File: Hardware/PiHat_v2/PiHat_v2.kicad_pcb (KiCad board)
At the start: 2 copper layers, 64 x 55 mm, 23 parts, among them P1 CONN_02X20, P2 CONN_01X02, P3 CONN_01X08

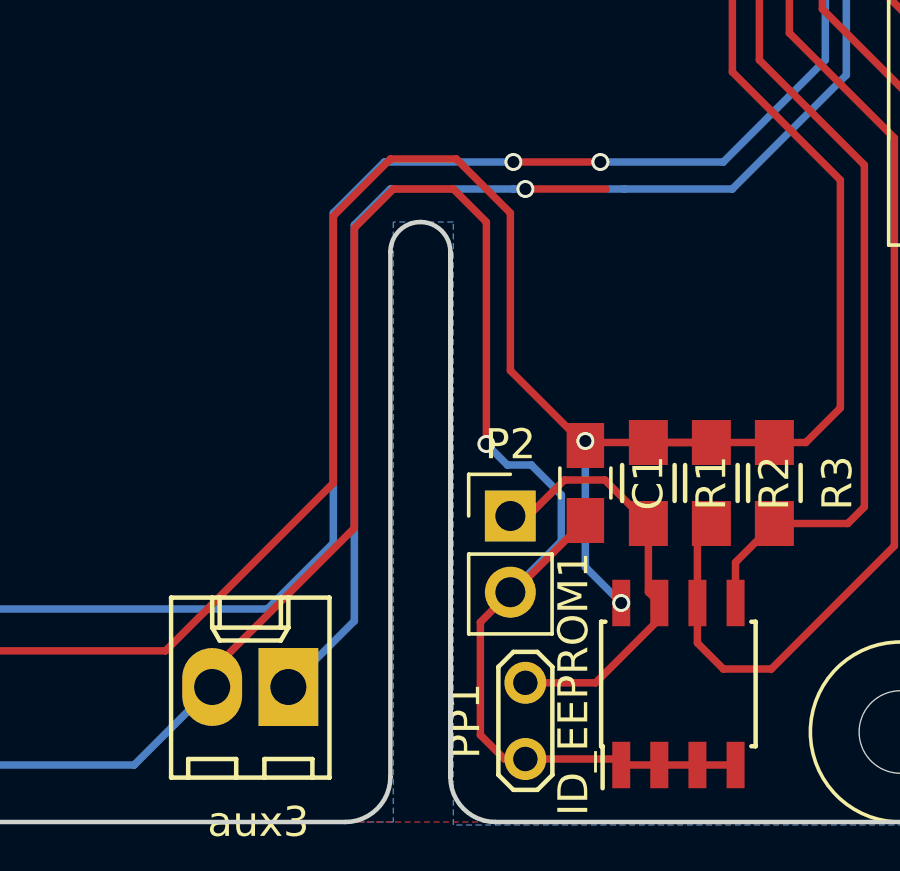
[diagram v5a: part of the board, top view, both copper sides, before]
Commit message: Insert Missing Via
I was missing a via in the lower right of the board - it has now been
re-inserted.
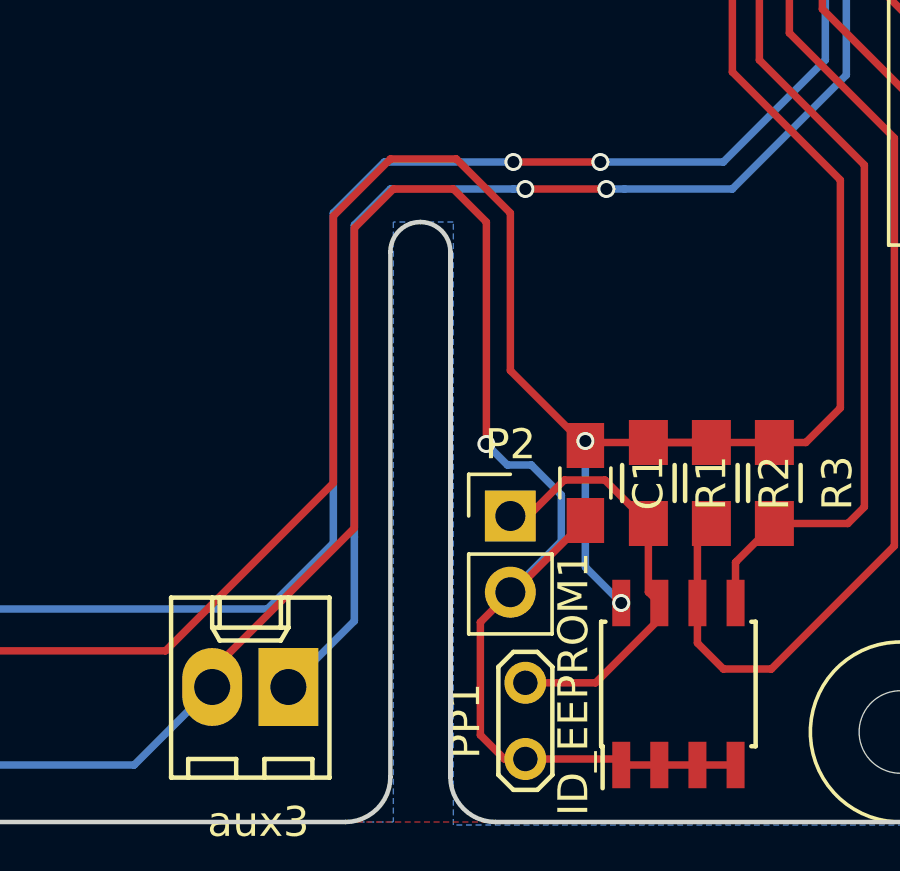
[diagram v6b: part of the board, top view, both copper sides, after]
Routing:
- net /GPIO5: vias 1 -> 2
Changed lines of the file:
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@@
   (general
     (links 56)
-    (no_connects 9)
+    (no_connects 8)
     (area 79.650001 53.1 168.85 129.200001)
     (thickness 1.6)
     (drawings 48)
-    (tracks 245)
+    (tracks 246)
     (zones 0)
     (modules 23)
@@
   (segment (start 96.2 72.2) (end 96.2 72.1) (width 0.25) (layer F.Cu) (net 1))
   (segment (start 96.2 72.1) (end 102 66.3) (width 0.25) (layer F.Cu) (net 1))
+  (segment (start 113.66 72.06) (end 112.16 70.56) (width 0.25) (layer F.Cu) (net 2))
+  (segment (start 112.16 70.56) (end 112.16 66.3) (width 0.25) (layer F.Cu) (net 2))
   (segment (start 118.5 115.1) (end 109.8 115.1) (width 0.25) (layer B.Cu) (net 2))
   (segment (start 109.8 115.1) (end 104.6 109.9) (width 0.25) (layer B.Cu) (net 2))
@@
   (segment (start 141 110.34) (end 142 109.34) (width 0.25) (layer F.Cu) (net 2))
   (segment (start 113.66 72.2) (end 113.66 72.06) (width 0.25) (layer F.Cu) (net 2))
-  (segment (start 113.66 72.06) (end 112.16 70.56) (width 0.25) (layer F.Cu) (net 2))
-  (segment (start 112.16 70.56) (end 112.16 66.3) (width 0.25) (layer F.Cu) (net 2))
   (segment (start 113.66 72.2) (end 113.5 72.2) (width 0.25) (layer B.Cu) (net 2))
   (segment (start 118.5 111.295) (end 114.495 111.295) (width 0.25) (layer F.Cu) (net 4))
@@
   (segment (start 149.1 111.9) (end 148.235 111.035) (width 0.25) (layer F.Cu) (net 22))
   (segment (start 148.235 111.035) (end 148.235 109.7) (width 0.25) (layer F.Cu) (net 22))
+  (via (at 145.2 95.9) (size 0.6) (drill 0.4) (layers F.Cu B.Cu) (net 23))
+  (segment (start 145.8 95.9) (end 145.2 95.9) (width 0.25) (layer B.Cu) (net 23))
+  (segment (start 149.4 95.9) (end 145.8 95.9) (width 0.25) (layer B.Cu) (net 23))
+  (segment (start 153.2 92.1) (end 149.4 95.9) (width 0.25) (layer B.Cu) (net 23))
+  (segment (start 153.2 80.3) (end 153.2 92.1) (width 0.25) (layer B.Cu) (net 23))
+  (segment (start 149.8 76.9) (end 153.2 80.3) (width 0.25) (layer B.Cu) (net 23))
+  (segment (start 145.6 76.9) (end 149.8 76.9) (width 0.25) (layer B.Cu) (net 23))
+  (segment (start 143.5 74.8) (end 145.6 76.9) (width 0.25) (layer B.Cu) (net 23))
+  (segment (start 143.5 71.9) (end 143.5 74.8) (width 0.25) (layer B.Cu) (net 23))
+  (segment (start 137.9 66.3) (end 143.5 71.9) (width 0.25) (layer B.Cu) (net 23))
+  (segment (start 142.5 95.9) (end 145.2 95.9) (width 0.25) (layer F.Cu) (net 23))
+  (segment (start 136.8 107.5) (end 136.8 110.3) (width 0.25) (layer B.Cu) (net 23))
+  (segment (start 136.8 110.3) (end 134.6 112.5) (width 0.25) (layer B.Cu) (net 23))
+  (segment (start 142.1 95.9) (end 138 95.9) (width 0.25) (layer B.Cu) (net 23))
+  (segment (start 142.5 95.9) (end 142.1 95.9) (width 0.25) (layer B.Cu) (net 23))
+  (segment (start 138 95.9) (end 136.8 97.1) (width 0.25) (layer B.Cu) (net 23))
+  (segment (start 136.8 97.1) (end 136.8 107.5) (width 0.25) (layer B.Cu) (net 23))
   (via (at 142.5 95.9) (size 0.6) (drill 0.4) (layers F.Cu B.Cu) (net 23))
-  (segment (start 136.8 97.1) (end 136.8 107.5) (width 0.25) (layer B.Cu) (net 23))
-  (segment (start 138 95.9) (end 136.8 97.1) (width 0.25) (layer B.Cu) (net 23))
-  (segment (start 142.5 95.9) (end 142.1 95.9) (width 0.25) (layer B.Cu) (net 23))
-  (segment (start 142.1 95.9) (end 138 95.9) (width 0.25) (layer B.Cu) (net 23))
-  (segment (start 134.6 112.5) (end 136.8 110.3) (width 0.25) (layer B.Cu) (net 23))
-  (segment (start 136.8 107.5) (end 136.8 110.3) (width 0.25) (layer B.Cu) (net 23))
-  (segment (start 142.5 95.9) (end 145.2 95.9) (width 0.25) (layer F.Cu) (net 23))
-  (segment (start 137.9 66.3) (end 143.5 71.9) (width 0.25) (layer B.Cu) (net 23))
-  (segment (start 143.5 71.9) (end 143.5 74.8) (width 0.25) (layer B.Cu) (net 23))
-  (segment (start 143.5 74.8) (end 145.6 76.9) (width 0.25) (layer B.Cu) (net 23))
-  (segment (start 145.6 76.9) (end 149.8 76.9) (width 0.25) (layer B.Cu) (net 23))
-  (segment (start 149.8 76.9) (end 153.2 80.3) (width 0.25) (layer B.Cu) (net 23))
-  (segment (start 153.2 80.3) (end 153.2 92.1) (width 0.25) (layer B.Cu) (net 23))
-  (segment (start 153.2 92.1) (end 149.4 95.9) (width 0.25) (layer B.Cu) (net 23))
-  (segment (start 149.4 95.9) (end 145.8 95.9) (width 0.25) (layer B.Cu) (net 23))
-  (segment (start 145.8 95.9) (end 145.2 95.9) (width 0.25) (layer B.Cu) (net 23))
   (segment (start 137.56 66.3) (end 137.9 66.3) (width 0.25) (layer B.Cu) (net 23))
   (segment (start 140.1 66.3) (end 143.2 69.4) (width 0.25) (layer B.Cu) (net 24))

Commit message: Finished PiHat v2 Design
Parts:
- removed LED1: Led_RGB_CA, LEDs:LED_Cree-PLCC4
- removed R4, R5, R6: R, Resistors_SMD:R_0805_HandSoldering
- added C2: 100n, Capacitors_SMD:C_0805_HandSoldering, F.Cu at (113.2, 78.3)
- added D1: D_Schottky, .pretty:Schottky_Diode, F.Cu at (108.6, 80.7)
- added P4: Neo_LED_RGB_IC, .pretty:Neo_RGB_LED, F.Cu at (111.8, 73.4)
- added aux5: CONN_01X02, Connectors_Molex:Molex_KK-6410-02_02x2.54mm_Straight, F.Cu at (152.0, 75.0)
- moved P3 38.1 mm to (118.0, 80.7)
- moved PP1 35.7 mm to (129.5, 81.6)
- moved C1 35.7 mm to (131.5, 72.4)
- moved R1 35.7 mm to (133.6, 72.4)
- moved R2 35.7 mm to (135.7, 72.4)
- moved R3 35.7 mm to (137.8, 72.4)
- moved ID_EEPROM1 35.0 mm to (135.0, 79.7)
- moved P2 34.2 mm to (128.0, 75.6), turned to 180 degrees
- moved aux4 30.3 mm to (152.0, 103.0), turned to 0 degrees
- moved temp1 24.8 mm to (99.0, 102.2)
- moved aux1 15.5 mm to (101.0, 75.2)
- moved aux2 15.3 mm to (108.0, 112.0), turned to 180 degrees
- moved S1 11.8 mm to (118.9, 109.0)
- moved aux3 0.78 mm to (134.0, 112.0)
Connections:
- P3 pad 1: /GPIO21 -> /GPIO27
- P3 pad 2: /GPIO20 -> /GPIO23
- P3 pad 3: /GPIO16 -> /GPIO22
- P3 pad 4: /GPIO12 -> /GPIO24
- P3 pad 5: /GPIO26 -> /GPIO10
- P3 pad 6: /GPIO19 -> /GPIO25
- P3 pad 7: /GPIO13 -> /GPIO9
- P3 pad 8: Net-(P3-Pad8) -> /GPIO8
- S1 pad 1: /GPIO7 -> /GPIO17
- aux1 pad 1: /GPIO18 -> /GPIO14
- aux2 pad 1: /GPIO17 -> /GPIO4
- aux3 pad 1: /GPIO5 -> /GPIO20
- aux4 pad 1: /GPIO6 -> /GPIO21
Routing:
- net /GPIO7: track 96.6 -> 0.00 mm, vias 2 -> 0
- net GND: track 159.1 -> 237.8 mm, vias 2 -> 3
- net /GPIO5: track 69.7 -> 0.34 mm, vias 2 -> 0
- net +3V3: track 122.9 -> 75.2 mm, vias 2 -> 3
- net /ID_SC: track 65.0 -> 21.8 mm
- net /GPIO8: track 0.00 -> 39.7 mm
- net /GPIO4: track 8.47 -> 48.1 mm
- net /ID_SD: track 54.4 -> 16.7 mm
- net /GPIO13: track 34.7 -> 0.00 mm
- net /GPIO20: track 21.6 -> 55.6 mm
- net /GPIO25: track 0.00 -> 33.6 mm
- net /GPIO9: track 0.00 -> 33.5 mm
- net /GPIO21: track 17.2 -> 50.1 mm
- net /GPIO12: track 31.6 -> 0.00 mm
- net /GPIO19: track 29.6 -> 0.22 mm
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
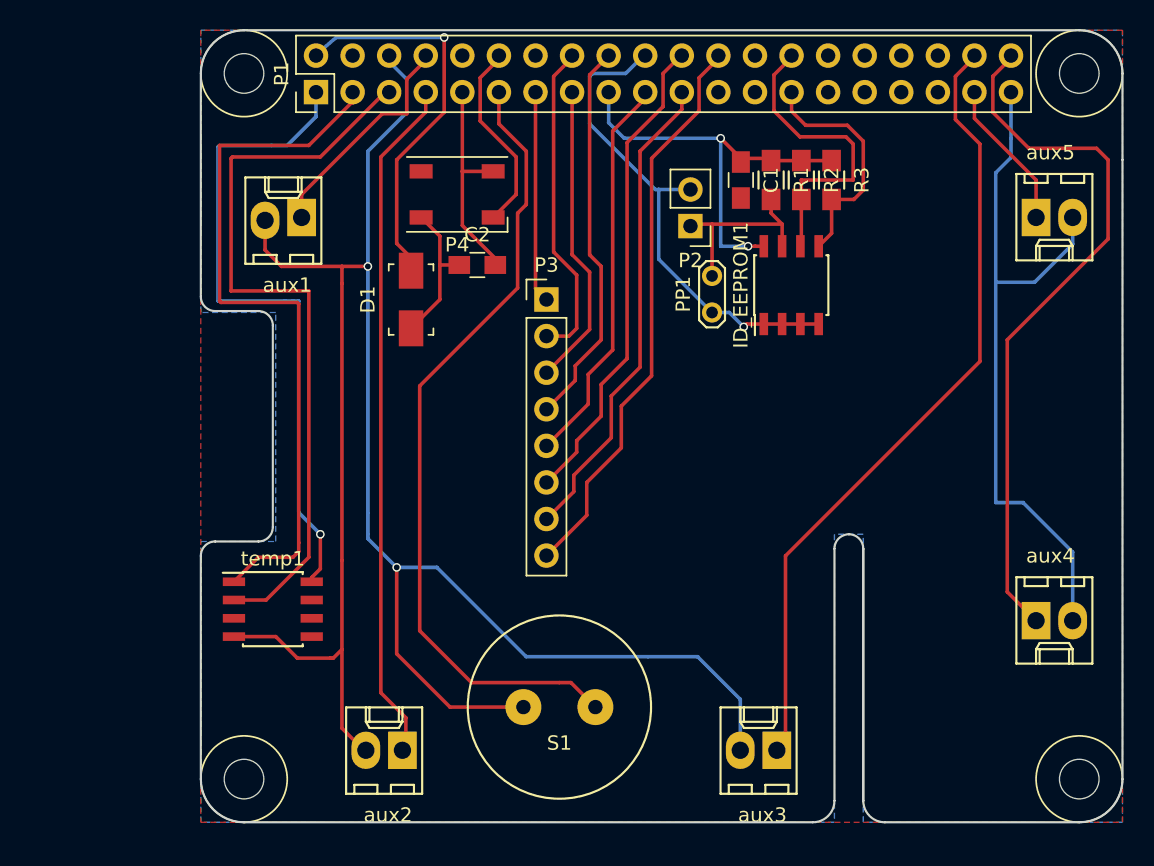
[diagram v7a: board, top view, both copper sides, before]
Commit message: Neopixel Footprint Fix
Rearranged the neopixel terminals to correctly mount it. Moved around
silk screen references and changed the text to better understand the
design when soldering. Added the developers' names to the back of the
board.
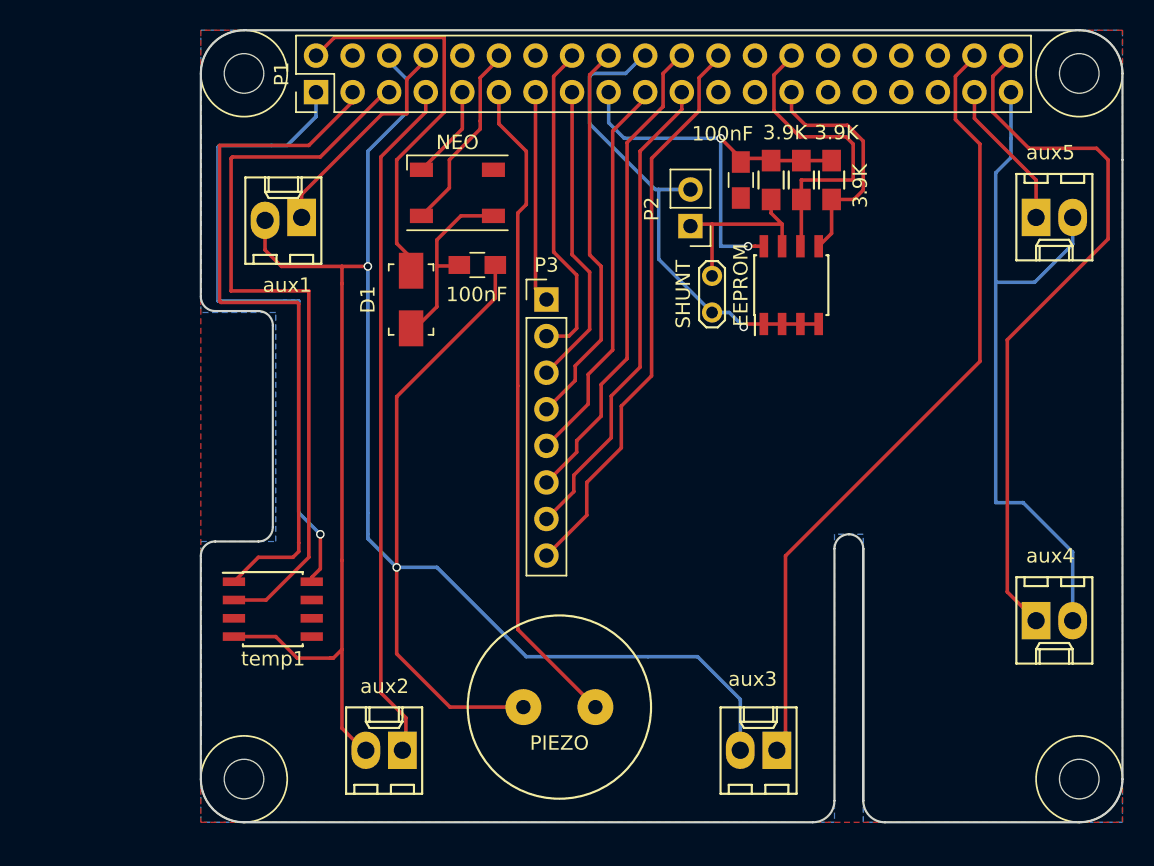
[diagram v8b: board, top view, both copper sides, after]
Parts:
- removed P4: Neo_LED_RGB_IC, .pretty:Neo_RGB_LED
- added NEO: Neo_LED_RGB_IC, .pretty:Neo_RGB_LED, F.Cu at (111.8, 73.3)
- renumbered C1 to 100nF, C2 to 100nF, R1 to 3.9K, R2 to 3.9K, R3 to 3.9K, ID_EEPROM1 to EEPROM, S1 to PIEZO, PP1 to SHUNT
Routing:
- net GND: track 237.8 -> 253.5 mm
- net /GPIO17: track 55.7 -> 46.1 mm
- net Net-(C2-Pad1): track 10.4 -> 13.3 mm
- net +5V: track 28.0 -> 28.1 mm, vias 1 -> 0
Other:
- board text added: "Clemson University CATS CI: Owen Phillips Stefan Abare Brice Grooms Brad Hord Giandre Acosta Maurice Barnett Garrett Ross Joshua McMillan Thor Brockman"
